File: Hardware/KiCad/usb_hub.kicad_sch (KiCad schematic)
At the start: 13 parts, among them J8 USB_A, U3 USBLC6-2SC6Y, U4 USB2422T/MJ, Y2 ABM8-24.000MHZ-B2-T

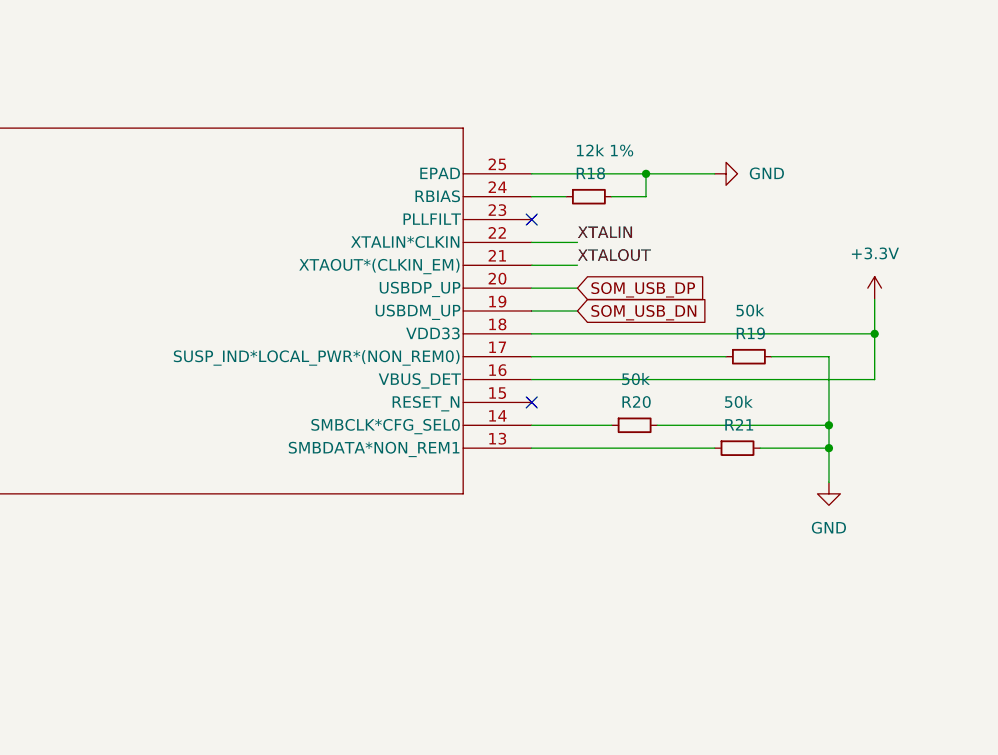
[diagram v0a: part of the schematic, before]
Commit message: Add switches for cpu reset and watchdog reset Add swtich for WWAN wirless disable Fix USB2422 VBUS-DET and NON_REM strap pins
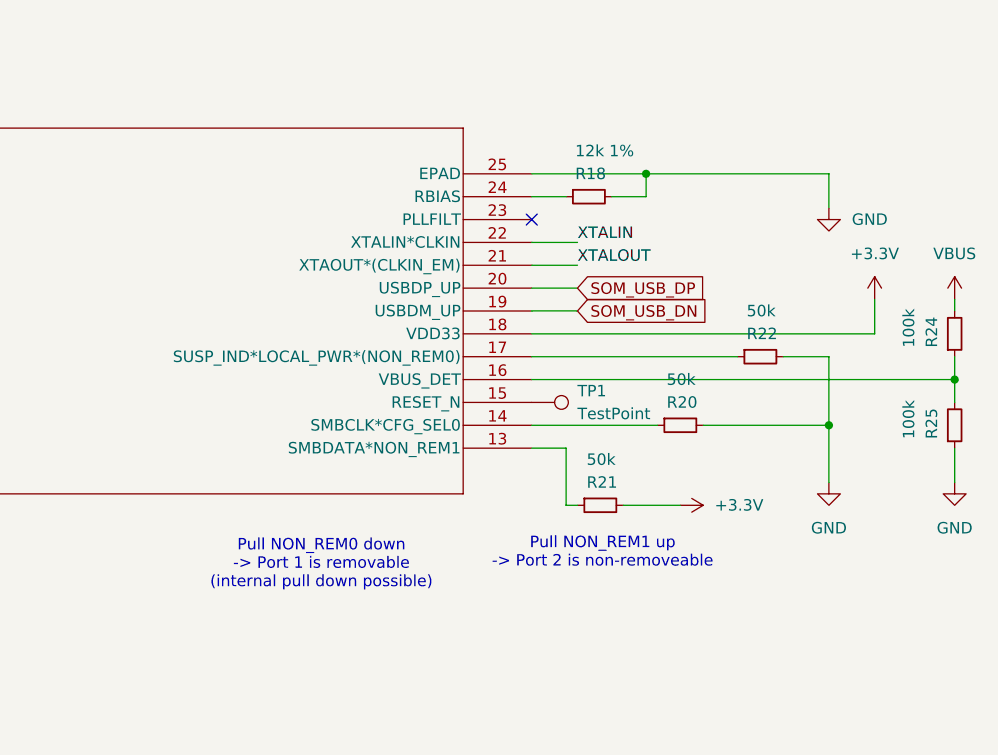
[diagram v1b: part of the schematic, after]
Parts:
- removed R19: 50k, Resistor_SMD:R_0402_1005Metric, symbol Device:R_Small
- added R22: 50k, Resistor_SMD:R_0402_1005Metric, symbol Device:R_Small
- added R24, R25: 100k, Resistor_SMD:R_0402_1005Metric, symbol Device:R_Small
- added TP1: TestPoint, TestPoint:TestPoint_Pad_D2.0mm, symbol Connector:TestPoint
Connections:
- net +3.3V: now also R21.2; no longer U4.16 (VBUS_DET)
- net GND: now also R22.2, R25.1; no longer R21.2
- net VBUS: now also R24.2
- net at U4.17 (SUSP_IND*LOCAL_PWR*(NON_REM0)): now also R22.1
- net at U4.15 (RESET_N): now also TP1.1
- new net: R24.1, R25.2, U4.16 (VBUS_DET)
- no-connect marks 6 -> 5
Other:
- note added: "Pull NON_REM0 down -> Port 1 is removable (internal pull down possible)"
- note added: "Pull NON_REM1 up -> Port 2 is non-removeable"
- moved on the sheet: R20, R21
